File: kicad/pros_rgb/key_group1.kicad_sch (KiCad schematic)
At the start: 14 parts

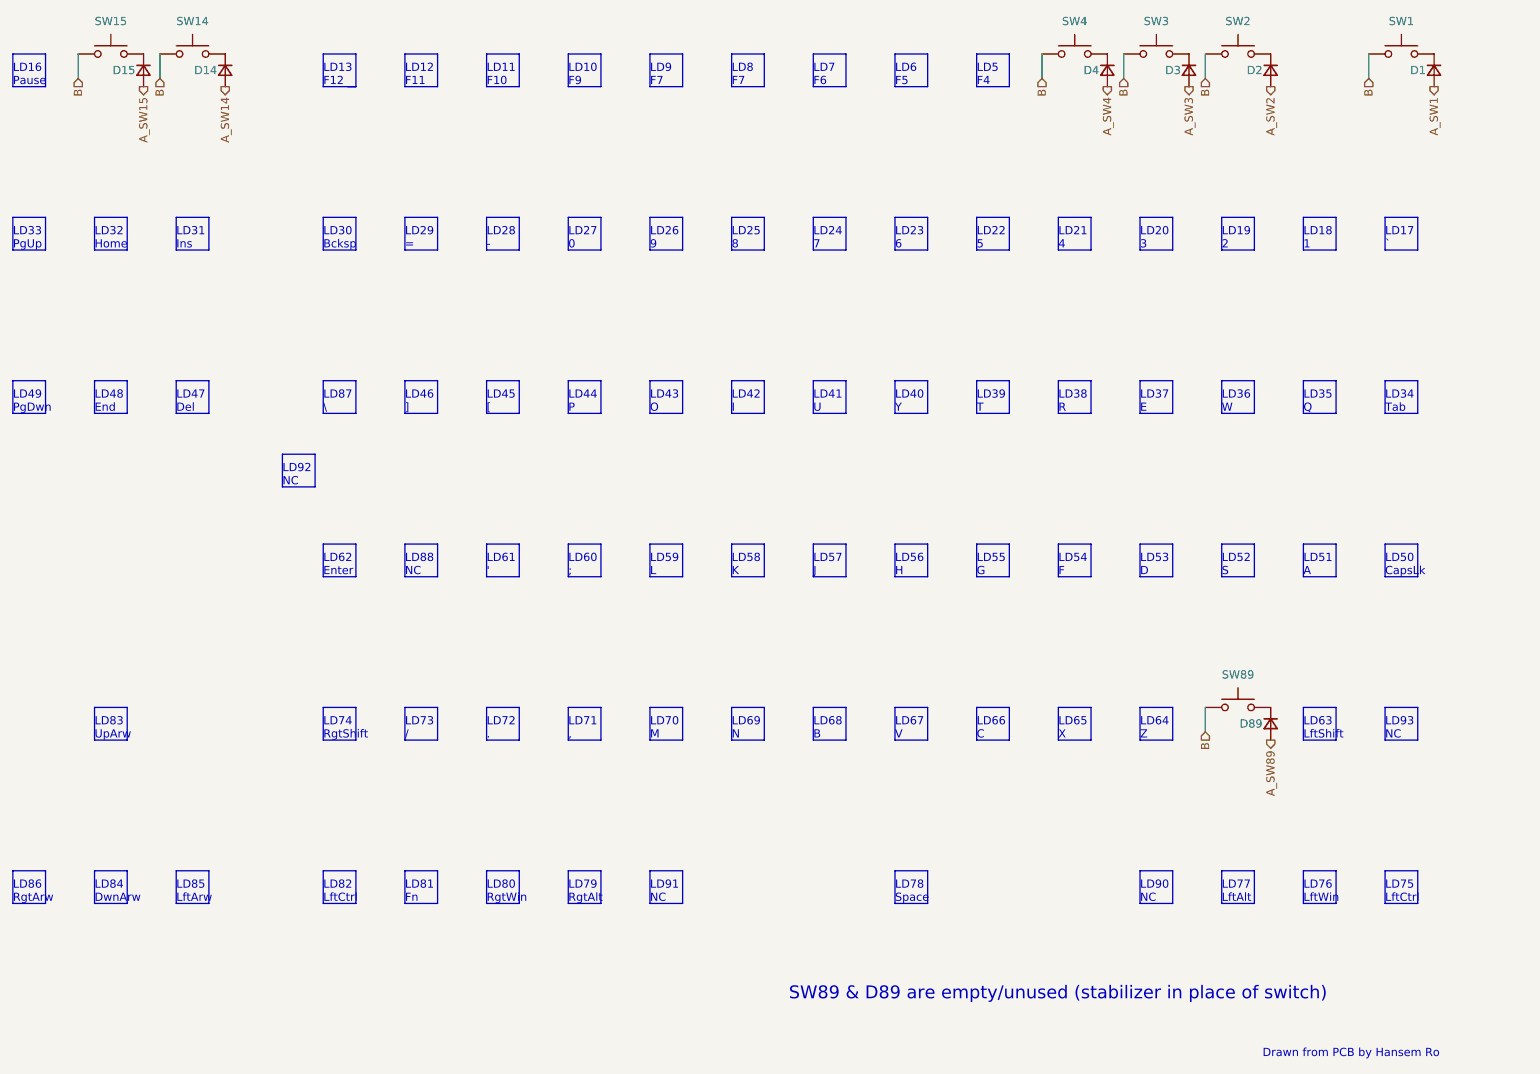
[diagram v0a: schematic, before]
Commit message: kicad/pros_rgb: update key groupings
These new groupings are based off ordering in firmware:
https://github.com/hansemro/pok3r_re_firmware/blob/4b68aa4baf7d28dc8dbf8eebcb1fdb59e7bcd629/disassemble/cmprosrgb/v122/cmprosrgb_v122.txt#L14599-L14629
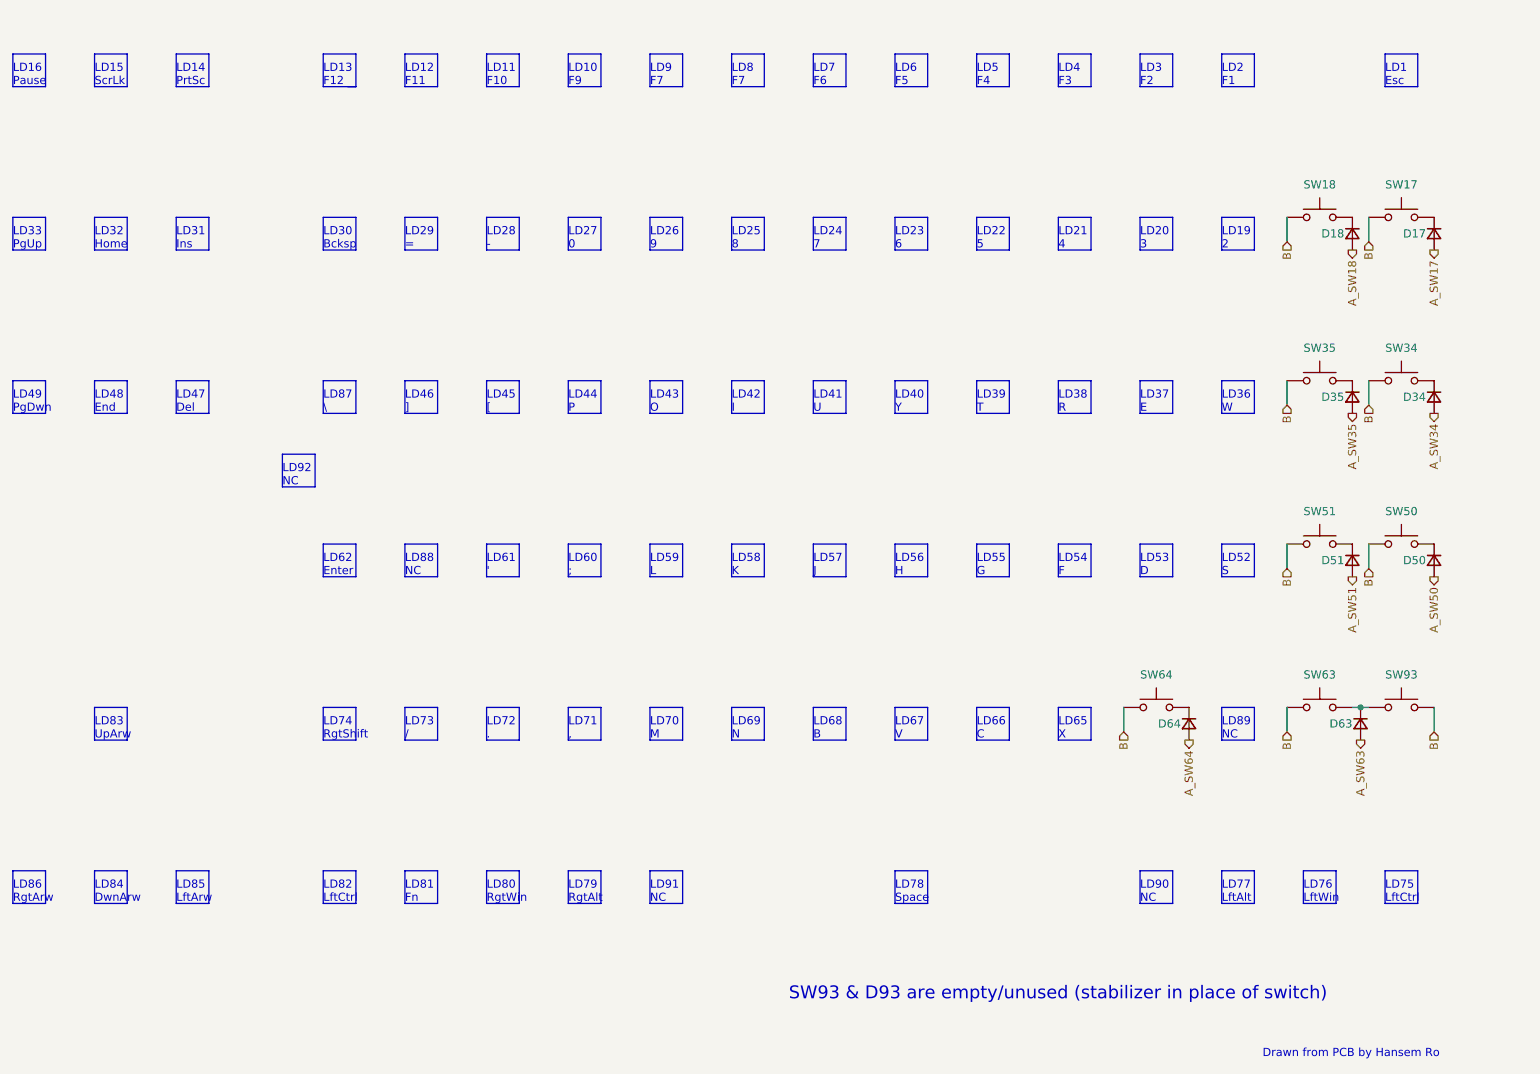
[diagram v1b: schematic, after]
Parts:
- removed D1, D14, D15, D2, D3, D4, D89: ~, symbol Device:D_Small
- removed SW1, SW14, SW15, SW2, SW3, SW4, SW89: ~, symbol Switch:SW_Push
- added D17, D18, D34, D35, D50, D51, D63, D64: (no value), symbol Device:D_Small
- added SW17, SW18, SW34, SW35, SW50, SW51, SW63, SW64, SW93: (no value), symbol Switch:SW_Push
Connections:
- net B: now also SW17.1, SW18.1, SW34.1, SW35.1, SW50.1, SW51.1, SW63.1, SW64.1, SW93.1
- new net: D64.1 (K), SW64.2
- new net: D34.1 (K), SW34.2
- new net: D18.1 (K), SW18.2
- new net: D35.1 (K), SW35.2
- new net: D50.1 (K), SW50.2
- new net: D51.1 (K), SW51.2
- new net: D17.1 (K), SW17.2
- new net: D63.1 (K), SW63.2, SW93.2
- new net A_SW17: D17.2 (A)
- new net A_SW18: D18.2 (A)
- new net A_SW34: D34.2 (A)
- new net A_SW35: D35.2 (A)
- new net A_SW50: D50.2 (A)
- new net A_SW51: D51.2 (A)
- new net A_SW63: D63.2 (A)
- new net A_SW64: D64.2 (A)
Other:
- note added: "LD1 Esc"
- note added: "LD14 PrtSc"
- note added: "LD15 ScrLk"
- note added: "LD2 F1"
- note added: "LD3 F2"
- note added: "LD4 F3"
- note added: "LD89 NC"
- note added: "SW93 & D93 are empty/unused (stabilizer in place of switch)"
- note removed: "LD17 `"
- note removed: "LD18 1"
- note removed: "LD34 Tab"
- note removed: "LD35 Q"
- note removed: "LD50 CapsLk"
- note removed: "LD51 A"
- note removed: "LD63 LftShift"
- note removed: "LD64 Z"
- note removed: "LD93 NC"
- note removed: "SW89 & D89 are empty/unused (stabilizer in place of switch)"

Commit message: kicad/pros_rgb: mark as Rev. B
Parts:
- D17, D18, D34, D35, D50, D51, D63, D64, SW17, SW18, SW34, SW35, SW50, SW51, SW63, SW64, SW93: value (none) -> ~
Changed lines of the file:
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@@
       (effects (font (size 1.27 1.27)) (justify right))
     )
-    (property "Value" "" (id 1) (at 243.84 129.5399 90)
+    (property "Value" "~" (id 1) (at 243.84 129.5399 90)
       (effects (font (size 1.27 1.27)) (justify left))
     )
@@
     (in_bom yes) (on_board yes)
     (property "Reference" "SW34" (id 0) (at 274.32 69.85 0))
-    (property "Value" "" (id 1) (at 274.32 69.85 0))
+    (property "Value" "~" (id 1) (at 274.32 69.85 0))
     (property "Footprint" "" (id 2) (at 274.32 69.85 0)
       (effects (font (size 1.27 1.27)) hide)
@@
     (in_bom yes) (on_board yes)
     (property "Reference" "SW18" (id 0) (at 261.62 44.45 0))
-    (property "Value" "" (id 1) (at 261.62 44.45 0))
+    (property "Value" "~" (id 1) (at 261.62 44.45 0))
     (property "Footprint" "" (id 2) (at 261.62 44.45 0)
       (effects (font (size 1.27 1.27)) hide)
@@
     (in_bom yes) (on_board yes)
     (property "Reference" "SW35" (id 0) (at 261.62 69.85 0))
-    (property "Value" "" (id 1) (at 261.62 69.85 0))
+    (property "Value" "~" (id 1) (at 261.62 69.85 0))
     (property "Footprint" "" (id 2) (at 261.62 69.85 0)
       (effects (font (size 1.27 1.27)) hide)
@@
     (in_bom yes) (on_board yes)
     (property "Reference" "SW64" (id 0) (at 236.22 120.65 0))
-    (property "Value" "" (id 1) (at 236.22 120.65 0))
+    (property "Value" "~" (id 1) (at 236.22 120.65 0))
     (property "Footprint" "" (id 2) (at 236.22 120.65 0)
       (effects (font (size 1.27 1.27)) hide)
@@
       (effects (font (size 1.27 1.27)) (justify right))
     )
-    (property "Value" "" (id 1) (at 281.94 104.1399 90)
+    (property "Value" "~" (id 1) (at 281.94 104.1399 90)
       (effects (font (size 1.27 1.27)) (justify left))
     )
@@
       (effects (font (size 1.27 1.27)) (justify right))
     )
-    (property "Value" "" (id 1) (at 269.24 78.7399 90)
+    (property "Value" "~" (id 1) (at 269.24 78.7399 90)
       (effects (font (size 1.27 1.27)) (justify left))
     )
@@
     (in_bom yes) (on_board yes)
     (property "Reference" "SW51" (id 0) (at 261.62 95.25 0))
-    (property "Value" "" (id 1) (at 261.62 95.25 0))
+    (property "Value" "~" (id 1) (at 261.62 95.25 0))
     (property "Footprint" "" (id 2) (at 261.62 95.25 0)
       (effects (font (size 1.27 1.27)) hide)
@@
     (in_bom yes) (on_board yes)
     (property "Reference" "SW50" (id 0) (at 274.32 95.25 0))
-    (property "Value" "" (id 1) (at 274.32 95.25 0))
+    (property "Value" "~" (id 1) (at 274.32 95.25 0))
     (property "Footprint" "" (id 2) (at 274.32 95.25 0)
       (effects (font (size 1.27 1.27)) hide)
@@
       (effects (font (size 1.27 1.27)) (justify right))
     )
-    (property "Value" "" (id 1) (at 281.94 78.7399 90)
+    (property "Value" "~" (id 1) (at 281.94 78.7399 90)
       (effects (font (size 1.27 1.27)) (justify left))
     )
@@
       (effects (font (size 1.27 1.27)) (justify right))
     )
-    (property "Value" "" (id 1) (at 269.24 53.3399 90)
+    (property "Value" "~" (id 1) (at 269.24 53.3399 90)
       (effects (font (size 1.27 1.27)) (justify left))
     )
@@
       (effects (font (size 1.27 1.27)) (justify right))
     )
-    (property "Value" "" (id 1) (at 281.94 53.3399 90)
+    (property "Value" "~" (id 1) (at 281.94 53.3399 90)
       (effects (font (size 1.27 1.27)) (justify left))
     )
@@
       (effects (font (size 1.27 1.27)) (justify right))
     )
-    (property "Value" "" (id 1) (at 270.51 129.5399 90)
+    (property "Value" "~" (id 1) (at 270.51 129.5399 90)
       (effects (font (size 1.27 1.27)) (justify left))
     )
@@
     (in_bom yes) (on_board yes)
     (property "Reference" "SW63" (id 0) (at 261.62 120.65 0))
-    (property "Value" "" (id 1) (at 261.62 120.65 0))
+    (property "Value" "~" (id 1) (at 261.62 120.65 0))
     (property "Footprint" "" (id 2) (at 261.62 120.65 0)
       (effects (font (size 1.27 1.27)) hide)
@@
     (in_bom yes) (on_board yes)
     (property "Reference" "SW17" (id 0) (at 274.32 44.45 0))
-    (property "Value" "" (id 1) (at 274.32 44.45 0))
+    (property "Value" "~" (id 1) (at 274.32 44.45 0))
     (property "Footprint" "" (id 2) (at 274.32 44.45 0)
       (effects (font (size 1.27 1.27)) hide)
@@
     (in_bom yes) (on_board yes)
     (property "Reference" "SW93" (id 0) (at 274.32 120.65 0))
-    (property "Value" "" (id 1) (at 274.32 120.65 0))
+    (property "Value" "~" (id 1) (at 274.32 120.65 0))
     (property "Footprint" "" (id 2) (at 274.32 120.65 0)
       (effects (font (size 1.27 1.27)) hide)
@@
       (effects (font (size 1.27 1.27)) (justify right))
     )
-    (property "Value" "" (id 1) (at 269.24 104.1399 90)
-      (effects (font (size 1.27 1.27)) (justify left))
-    )
+    (property "Value" "~" (id 1) (at 269.24 104.1399 90)
+      (effects (font (size 1.27 1.27)) (justify left))
+    )

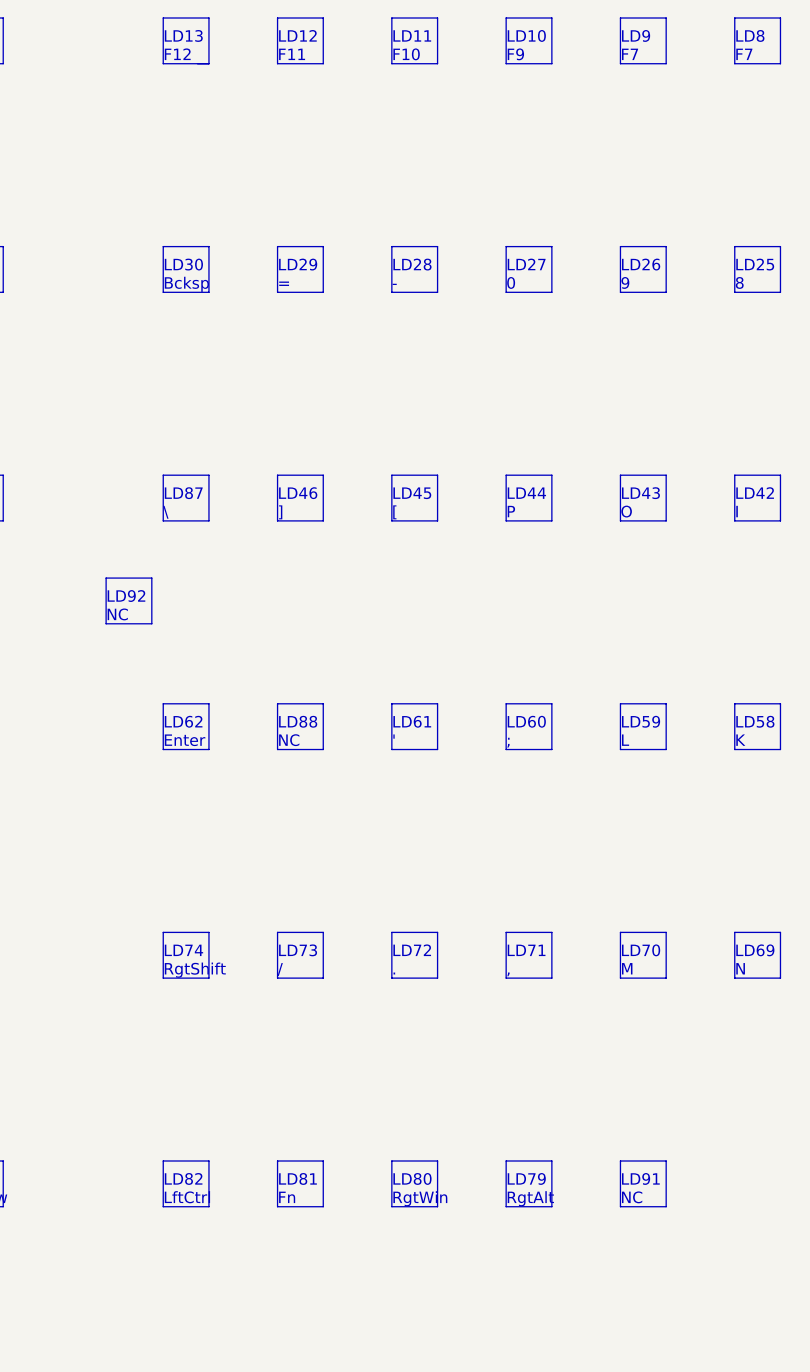
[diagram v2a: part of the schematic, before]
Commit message: kicad/pros_rgb: fix typos
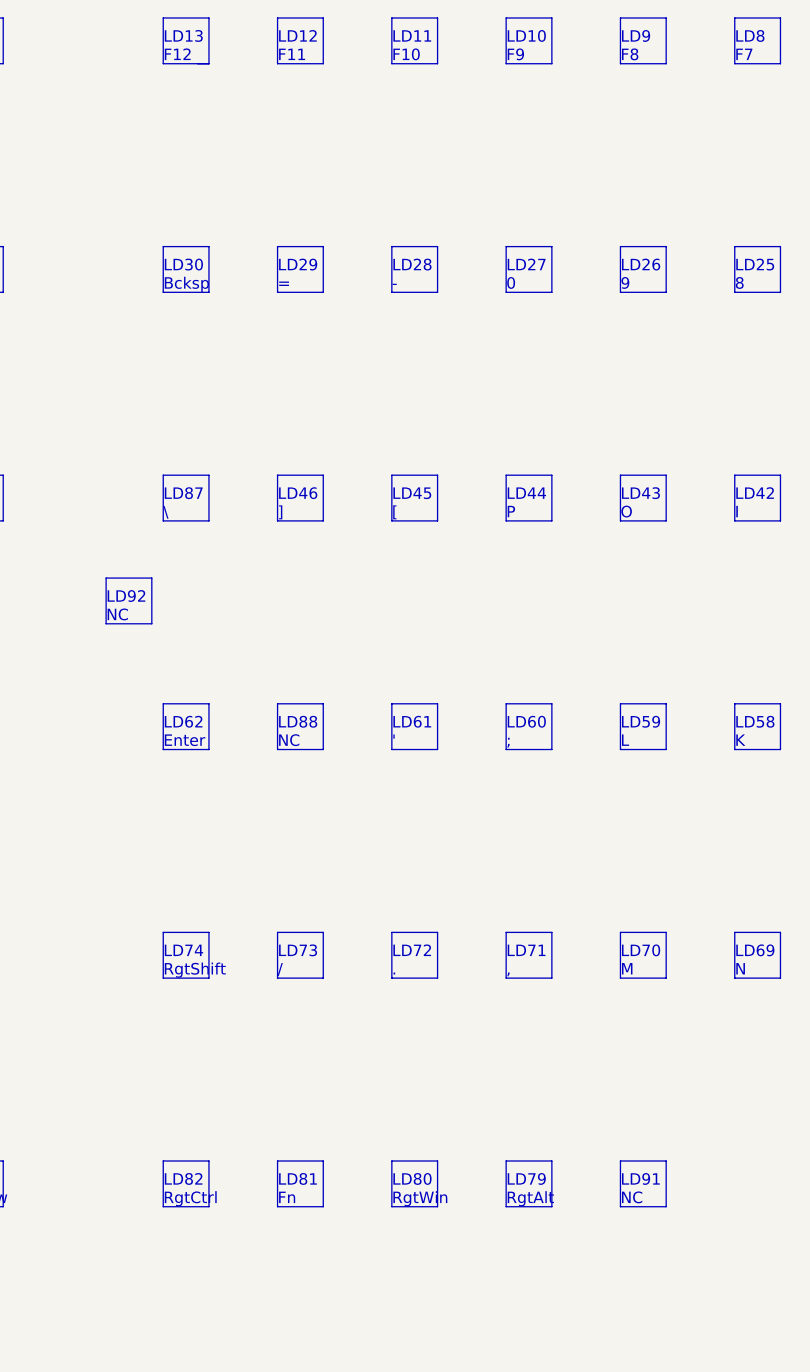
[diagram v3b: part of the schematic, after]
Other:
- note added: "LD82 RgtCtrl"
- note added: "LD9 F8"
- note removed: "LD82 LftCtrl"
- note removed: "LD9 F7"
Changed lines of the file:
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@@
     (effects (font (size 1.27 1.27)) (justify left bottom))
   )
-  (text "LD9\nF7" (at 157.48 29.21 0)
+  (text "LD9\nF8" (at 157.48 29.21 0)
     (effects (font (size 1.27 1.27)) (justify left bottom))
   )
@@
     (effects (font (size 1.27 1.27)) (justify left bottom))
   )
-  (text "LD82\nLftCtrl" (at 106.68 156.21 0)
+  (text "LD82\nRgtCtrl" (at 106.68 156.21 0)
     (effects (font (size 1.27 1.27)) (justify left bottom))
   )
